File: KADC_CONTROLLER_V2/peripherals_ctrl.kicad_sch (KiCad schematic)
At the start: 82 parts

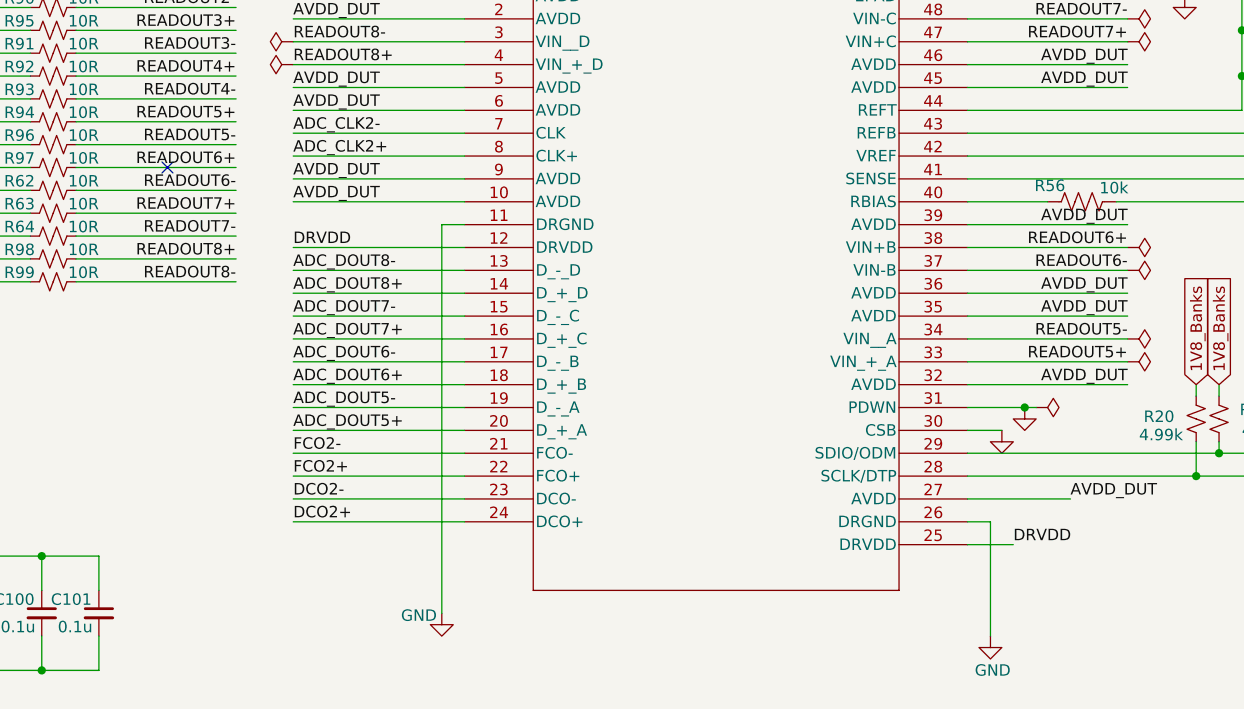
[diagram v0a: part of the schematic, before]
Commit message: Many Updates
Starting new power sequence and implementing KR260 PS circuitry.
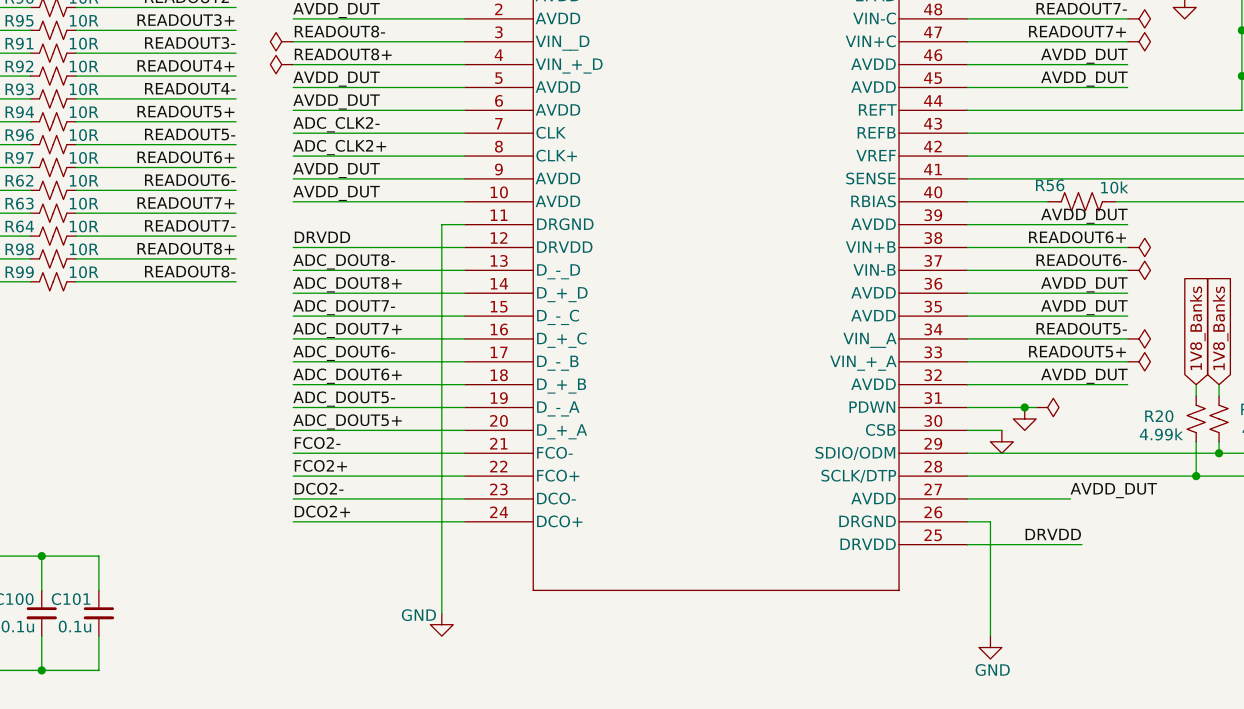
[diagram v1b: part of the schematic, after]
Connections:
- no-connect marks 1 -> 0
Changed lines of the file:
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@@
 		(color 0 0 0 0)
 	)
-	(no_connect
-		(at 99.06 124.46)
-	)
 	(wire
 		(pts
@@
 	(wire
 		(pts
-			(xy 193.04 166.37) (xy 187.96 166.37)
+			(xy 200.66 166.37) (xy 187.96 166.37)
 		)
 		(stroke
@@
 	)
 	(label "DRVDD"
-		(at 193.04 166.37 0)
+		(at 200.66 166.37 180)
 		(effects
 			(font
 				(size 1.27 1.27)
 			)
-			(justify left bottom)
+			(justify right bottom)
 		)
 	)
